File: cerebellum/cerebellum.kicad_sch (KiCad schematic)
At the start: 25 parts, among them J1 GPIO, J2 Conn_MOTA, J3 Conn_MOTB, J4 MD_POW, J5 Conn_SPI, J6 Conn_UART, J7 Conn_I2C, J8 VBUS(OUT), SW1 SW_PULLUP, SW2 SW_PULLDOWN, SW3 SW_SPDT, U1 CAT24C256, U2 POLOLU_TB6612_CARRIER, U3 HC-SR04

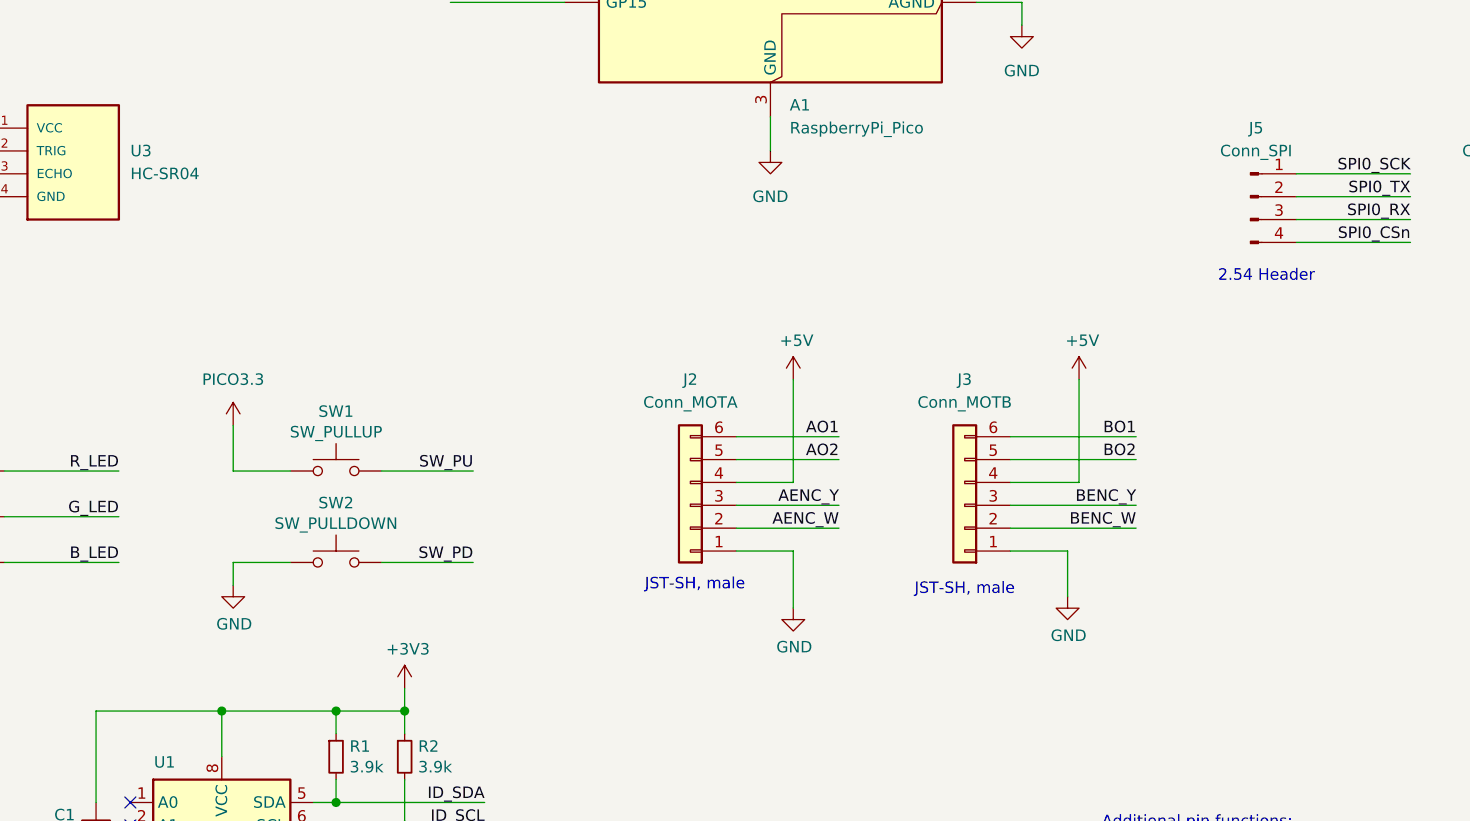
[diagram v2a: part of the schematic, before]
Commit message: update schematic
debounce switches
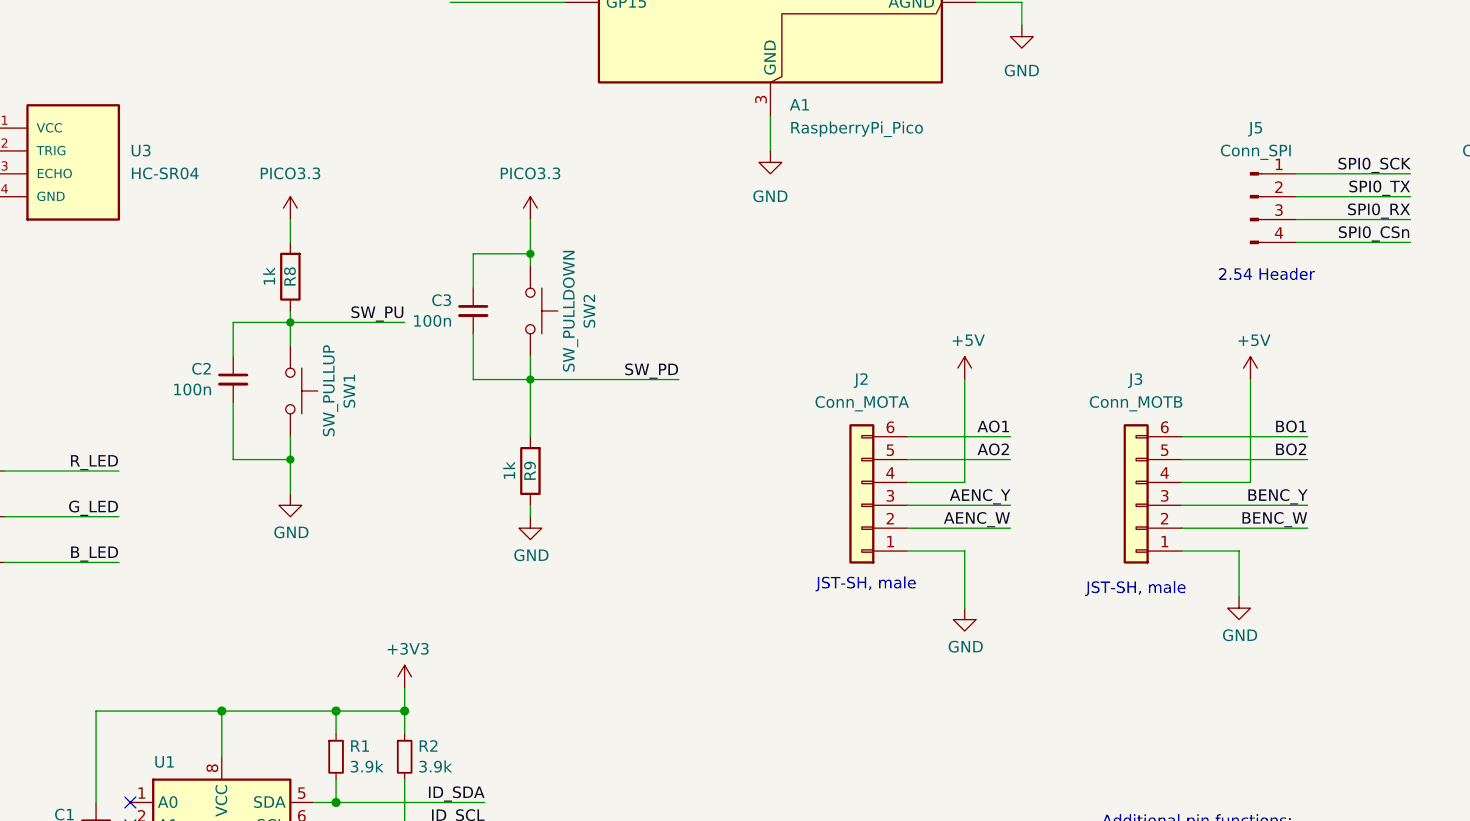
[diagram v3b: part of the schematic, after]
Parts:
- added C2, C3: 100n, Capacitor_SMD:C_0805_2012Metric_Pad1.18x1.45mm_HandSolder, symbol Device:C_Small
- added R8, R9: 1k, Resistor_SMD:R_1206_3216Metric_Pad1.30x1.75mm_HandSolder, symbol Device:R
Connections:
- net GND: now also SW1.2, C2.2, R9.1; no longer SW2.1
- net PICO3.3: now also SW2.1, C3.1, R8.2; no longer SW1.1
- net SW_PD: now also C3.2, R9.2
- net SW_PU: now also SW1.1, C2.1, R8.1; no longer SW1.2
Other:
- moved on the sheet: J2, J3, SW1, SW2

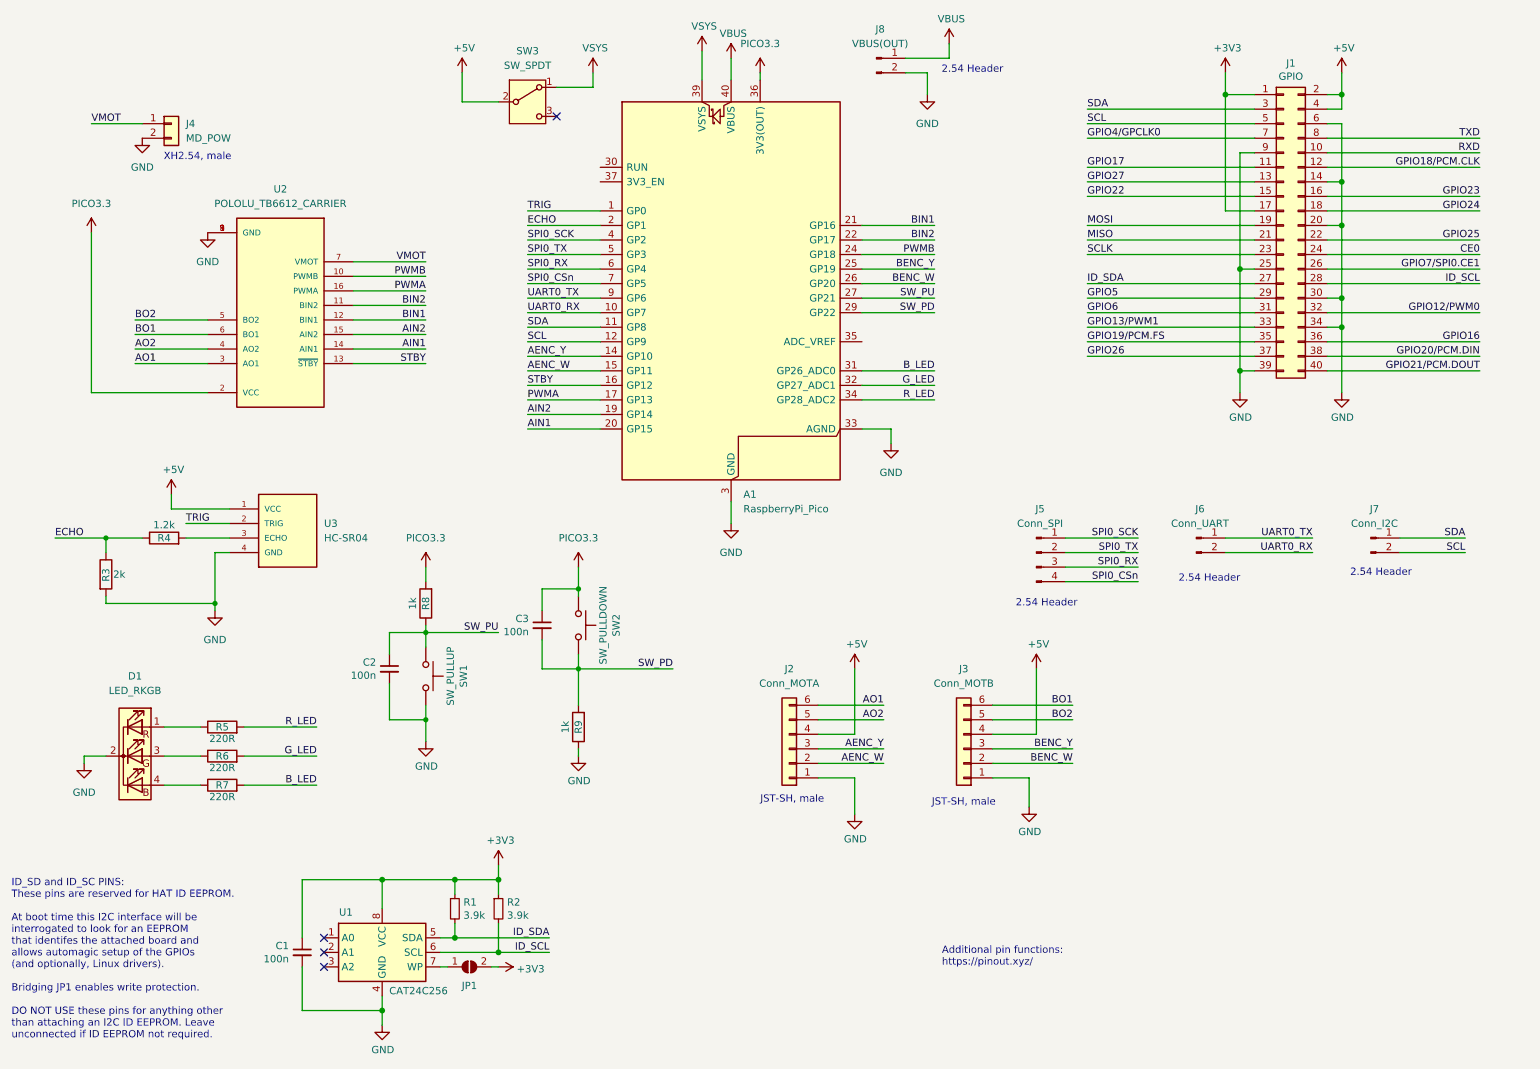
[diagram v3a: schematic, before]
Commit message: update design
wire up
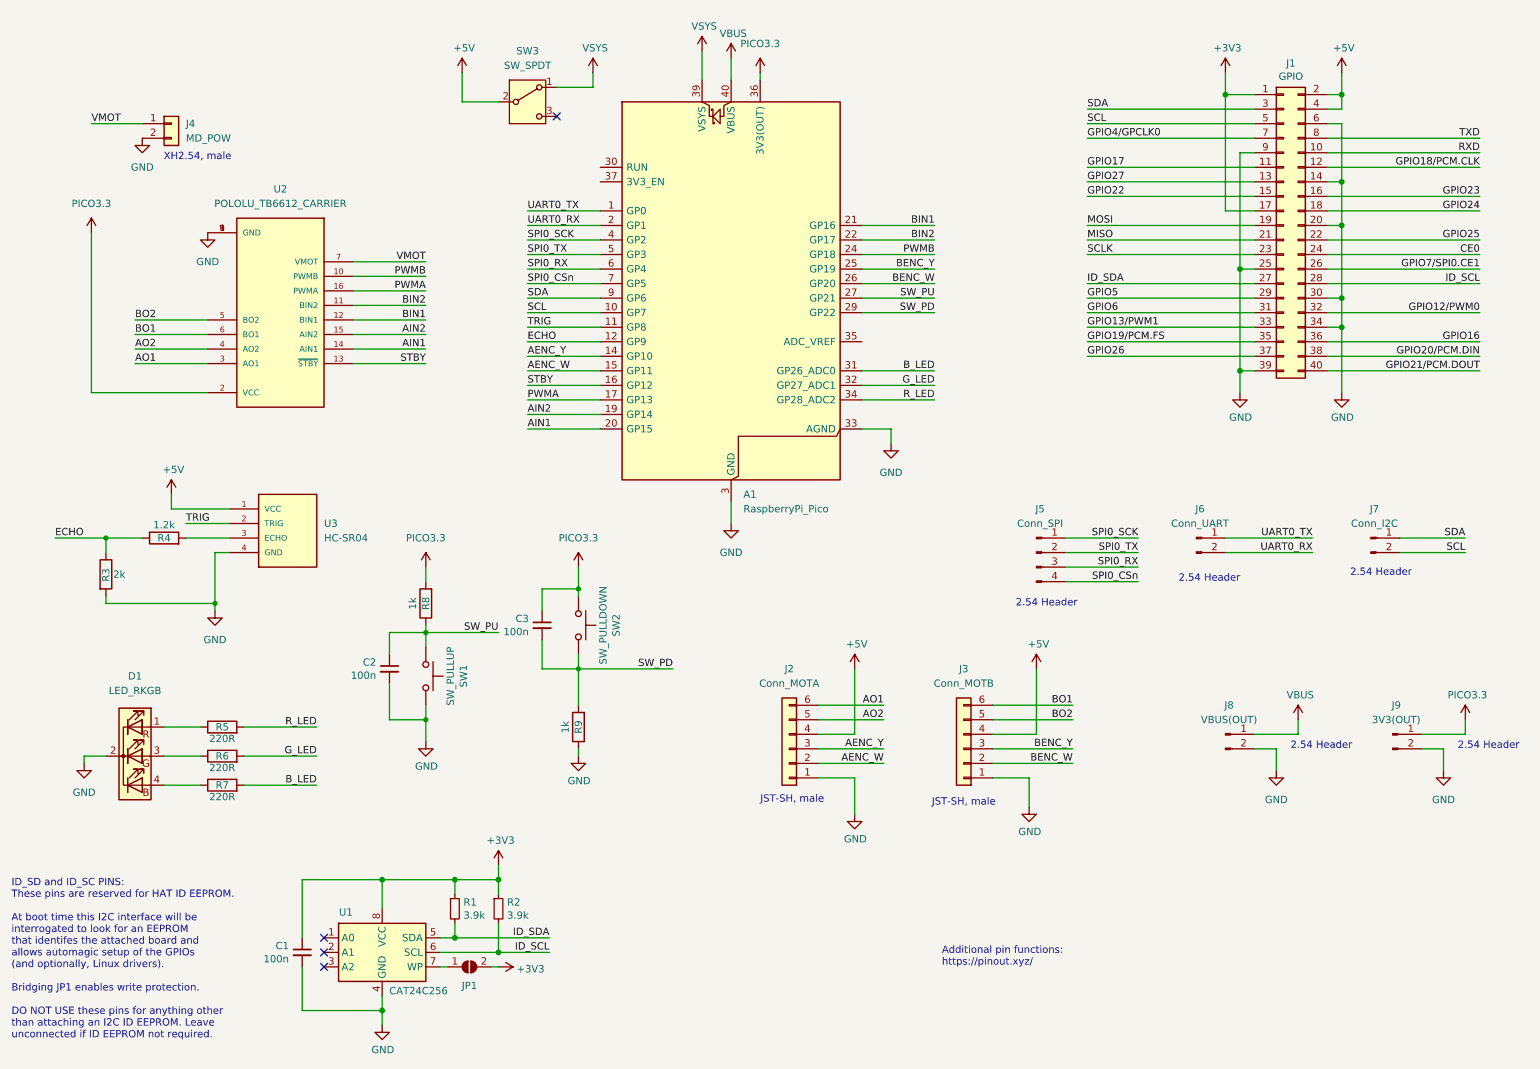
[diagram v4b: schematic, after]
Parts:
- added J9: 3V3(OUT), Connector_PinHeader_2.54mm:PinHeader_1x02_P2.54mm_Vertical, symbol Connector:Conn_01x02_Pin
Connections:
- net ECHO: now also A1.12 (GP9); no longer A1.2 (GP1)
- net GND: now also J9.2 (Pin_2)
- net PICO3.3: now also J9.1 (Pin_1)
- net SCL: now also A1.10 (GP7); no longer A1.12 (GP9)
- net SDA: now also A1.9 (GP6); no longer A1.11 (GP8)
- net TRIG: now also A1.11 (GP8); no longer A1.1 (GP0)
- net UART0_RX: now also A1.2 (GP1); no longer A1.10 (GP7)
- net UART0_TX: now also A1.1 (GP0); no longer A1.9 (GP6)
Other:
- moved on the sheet: J8

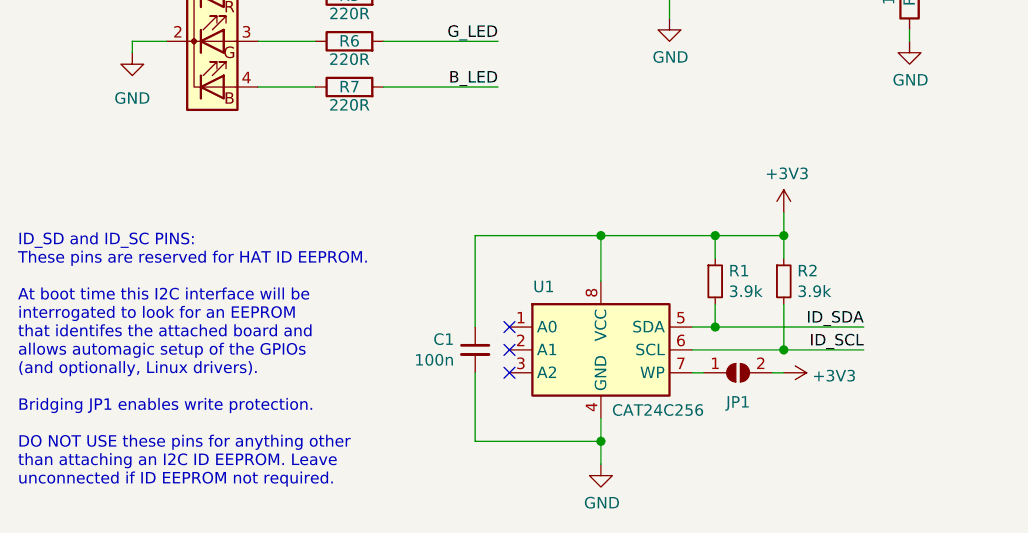
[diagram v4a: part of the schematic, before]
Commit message: remove eeprom from schematic
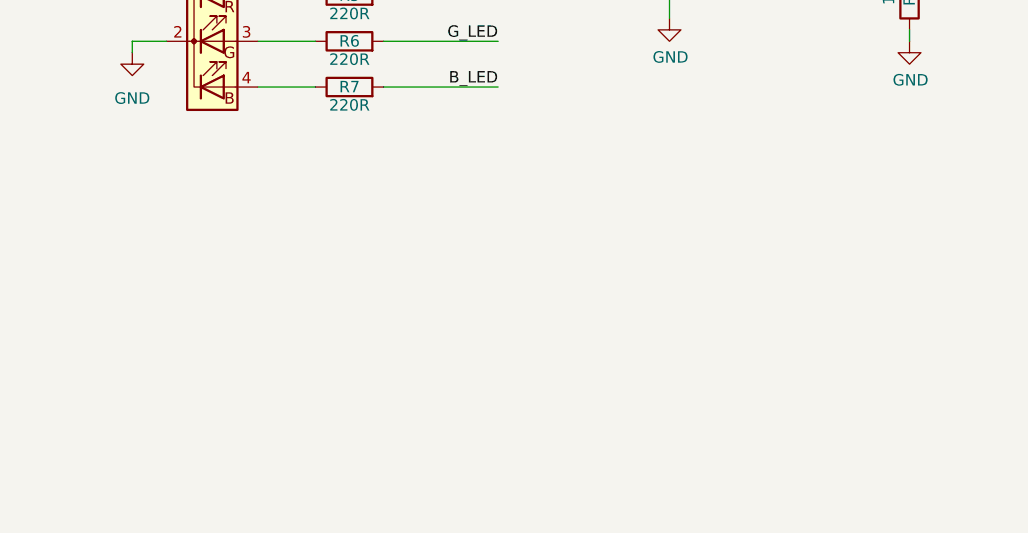
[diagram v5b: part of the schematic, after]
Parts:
- removed C1: 100n, symbol Device:C_Small
- removed JP1: ID_WP, symbol Jumper:SolderJumper_2_Open
- removed R1, R2: 3.9k, symbol Device:R_Small
- removed U1: CAT24C256, symbol Memory_EEPROM:CAT24C256
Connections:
- no-connect marks 4 -> 1
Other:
- note removed: "ID_SD and ID_SC PINS: These pins are reserved for HAT ID EEPROM. At boot time this I2C interface will be interrogated to look for an EEPROM that identifes the attached board and allows automagic setup of the GPIOs (and optionally, Linux drivers). Bridging JP1 enables write protection. DO NOT USE these pins for anything other than attaching an I2C ID EEPROM. Leave unconnected if ID EEPROM not requ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"

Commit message: update footprints
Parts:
- D1: footprint LED_THT:LED_D5.0mm-4_RGB -> LED_THT:LED_D5.0mm-4_RGB_Wide_Pins
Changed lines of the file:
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@@
 			)
 		)
-		(property "Footprint" "LED_THT:LED_D5.0mm-4_RGB"
+		(property "Footprint" "LED_THT:LED_D5.0mm-4_RGB_Wide_Pins"
 			(at 38.1 144.78 0)
 			(effects

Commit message: adjust layout
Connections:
- net GND: now also J4.1 (Pin_1); no longer J4.2 (Pin_2)
- net VMOT: now also J4.2 (Pin_2); no longer J4.1 (Pin_1)
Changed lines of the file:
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@@
 	(wire
 		(pts
+			(xy 38.1 33.02) (xy 39.37 33.02)
+		)
+		(stroke
+			(width 0)
+			(type default)
+		)
+	)
+	(wire
+		(pts
 			(xy 165.1 63.5) (xy 177.8 63.5)
 		)
@@
 	(wire
 		(pts
-			(xy 30.48 33.02) (xy 39.37 33.02)
+			(xy 38.1 33.02) (xy 38.1 39.37)
 		)
 		(stroke
@@
 	(wire
 		(pts
+			(xy 30.48 35.56) (xy 39.37 35.56)
+		)
+		(stroke
+			(width 0)
+			(type default)
+		)
+	)
+	(wire
+		(pts
 			(xy 157.48 144.78) (xy 168.91 144.78)
 		)
@@
 		)
 	)
+	(label "VMOT"
+		(at 30.48 35.56 0)
+		(effects
+			(font
+				(size 1.27 1.27)
+			)
+			(justify left bottom)
+		)
+	)
 	(label "AENC_Y"
 		(at 106.68 73.66 0)
@@
 		)
 	)
-	(label "VMOT"
-		(at 30.48 33.02 0)
-		(effects
-			(font
-				(size 1.27 1.27)
-			)
-			(justify left bottom)
-		)
-	)
 	(label "SW_PU"
 		(at 101.6 121.92 180)
@@
 		(lib_name "GND_1")
 		(lib_id "power:GND")
-		(at 39.37 35.56 0)
+		(at 38.1 39.37 0)
 		(unit 1)
 		(exclude_from_sim no)
@@
 		(fields_autoplaced yes)
 		(property "Reference" "#PWR025"
-			(at 39.37 41.91 0)
+			(at 38.1 45.72 0)
 			(effects
 				(font
@@
 		)
 		(property "Value" "GND"
-			(at 39.37 40.64 0)
+			(at 38.1 44.45 0)
 			(effects
 				(font
@@
 		)
 		(property "Footprint" ""
-			(at 39.37 35.56 0)
+			(at 38.1 39.37 0)
 			(effects
 				(font
@@
 		)
 		(property "Datasheet" ""
-			(at 39.37 35.56 0)
+			(at 38.1 39.37 0)
 			(effects
 				(font
@@
 		)
 		(property "Description" "Power symbol creates a global label with name \"GND\" , ground"
-			(at 39.37 35.56 0)
+			(at 38.1 39.37 0)
 			(effects
 				(font

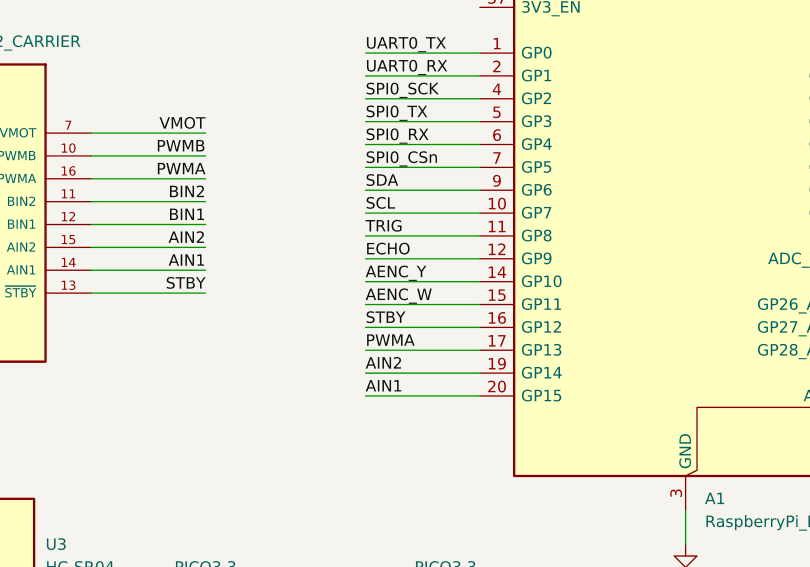
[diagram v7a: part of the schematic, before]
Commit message: update wiring
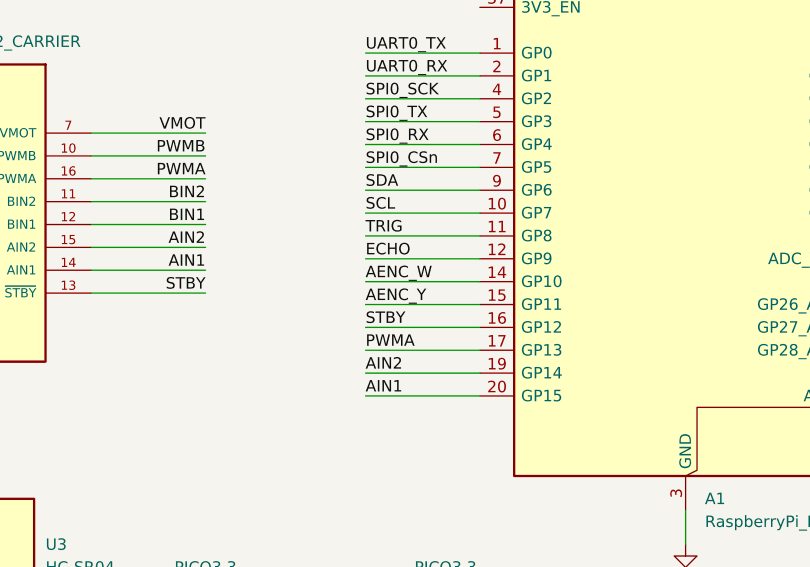
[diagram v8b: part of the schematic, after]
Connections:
- net AENC_W: now also A1.14 (GP10); no longer A1.15 (GP11)
- net AENC_Y: now also A1.15 (GP11); no longer A1.14 (GP10)
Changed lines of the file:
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@@
-		)
-	)
-	(label "AENC_W"
-		(at 106.68 76.2 0)
-		(effects
-			(font
-				(size 1.27 1.27)
-			)
-			(justify left bottom)
 		)
 	)
@@
 		)
 	)
+	(label "AENC_Y"
+		(at 106.68 76.2 0)
+		(effects
+			(font
+				(size 1.27 1.27)
+			)
+			(justify left bottom)
+		)
+	)
 	(label "PWMB"
 		(at 88.9 59.69 180)
@@
 		)
 	)
-	(label "AENC_Y"
-		(at 106.68 73.66 0)
-		(effects
-			(font
-				(size 1.27 1.27)
-			)
-			(justify left bottom)
-		)
-	)
 	(label "GPIO25"
 		(at 273.05 53.34 180)
@@
 		)
 	)
+	(label "AENC_W"
+		(at 106.68 73.66 0)
+		(effects
+			(font
+				(size 1.27 1.27)
+			)
+			(justify left bottom)
+		)
+	)
